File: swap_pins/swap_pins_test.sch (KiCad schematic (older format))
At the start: 6 parts, among them U101 PIC18F452-IP

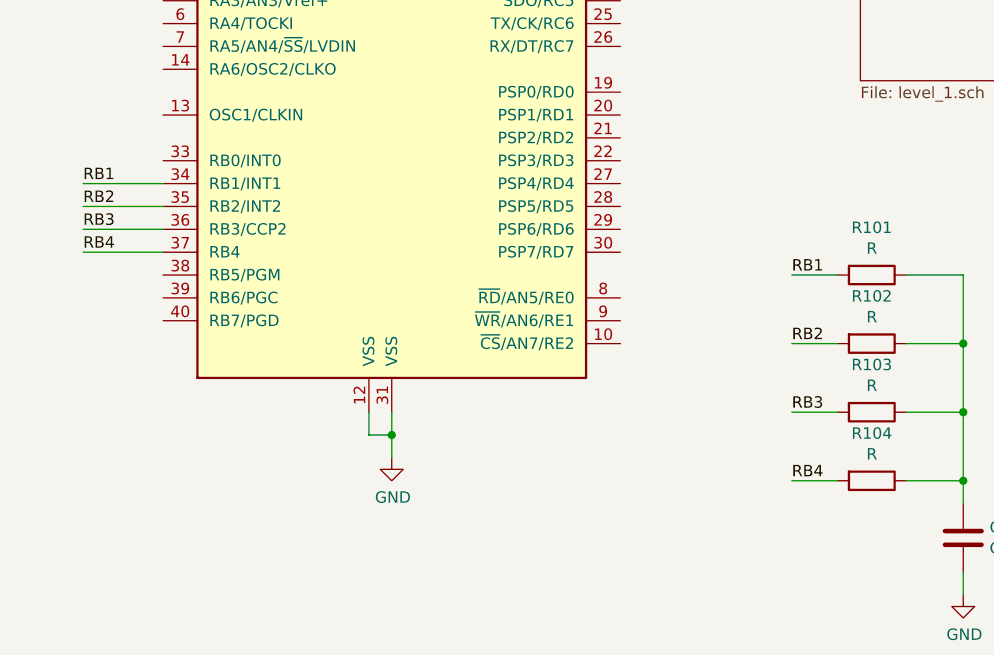
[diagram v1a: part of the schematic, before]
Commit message: changed project to include hierarchical labels also
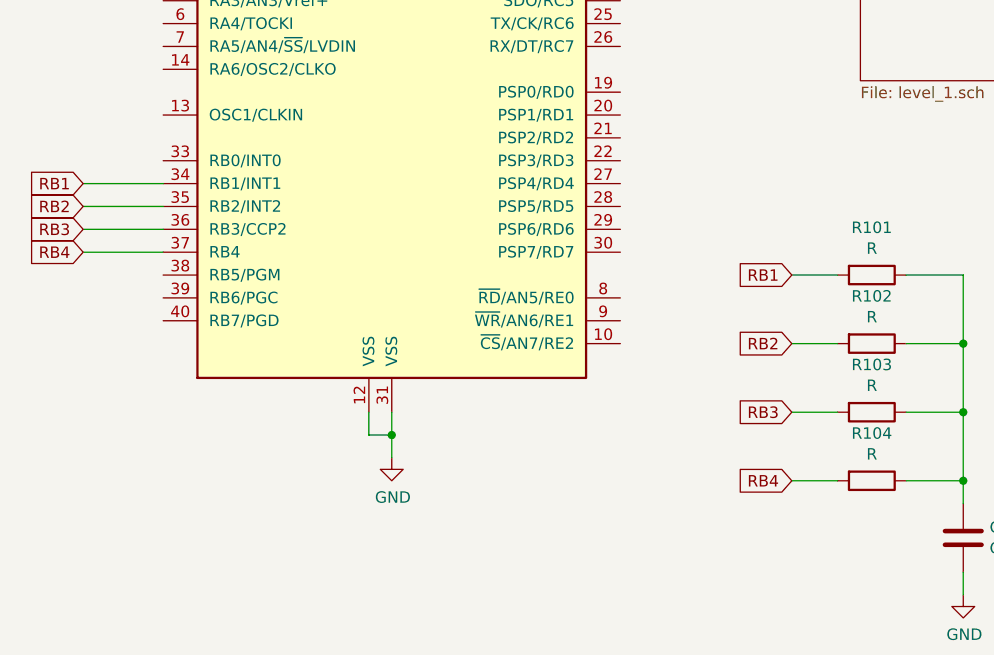
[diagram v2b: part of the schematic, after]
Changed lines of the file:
@@
 	5800 4300 5800 4600
 Connection ~ 5800 4600
-Text Label 5050 4300 0    50   ~ 0
-RB1
-Text Label 5050 4600 0    50   ~ 0
-RB2
-Text Label 5050 4900 0    50   ~ 0
-RB3
-Text Label 5050 5200 0    50   ~ 0
-RB4
 $Comp
 L power:GND #PWR0103
@@
 Wire Wire Line
 	2300 4200 1950 4200
-Text Label 1950 3900 0    50   ~ 0
-RB1
-Text Label 1950 4000 0    50   ~ 0
-RB2
-Text Label 1950 4100 0    50   ~ 0
-RB3
-Text Label 1950 4200 0    50   ~ 0
-RB4
 Wire Wire Line
 	3200 4900 3200 5000
@@
 	1    0    0    -1
 $EndComp
+Text GLabel 1950 3900 0    50   Input ~ 0
+RB1
+Text GLabel 1950 4000 0    50   Input ~ 0
+RB2
+Text GLabel 1950 4100 0    50   Input ~ 0
+RB3
+Text GLabel 1950 4200 0    50   Input ~ 0
+RB4
+Text GLabel 5050 4300 0    50   Input ~ 0
+RB1
+Text GLabel 5050 4600 0    50   Input ~ 0
+RB2
+Text GLabel 5050 4900 0    50   Input ~ 0
+RB3
+Text GLabel 5050 5200 0    50   Input ~ 0
+RB4
 $EndSCHEMATC

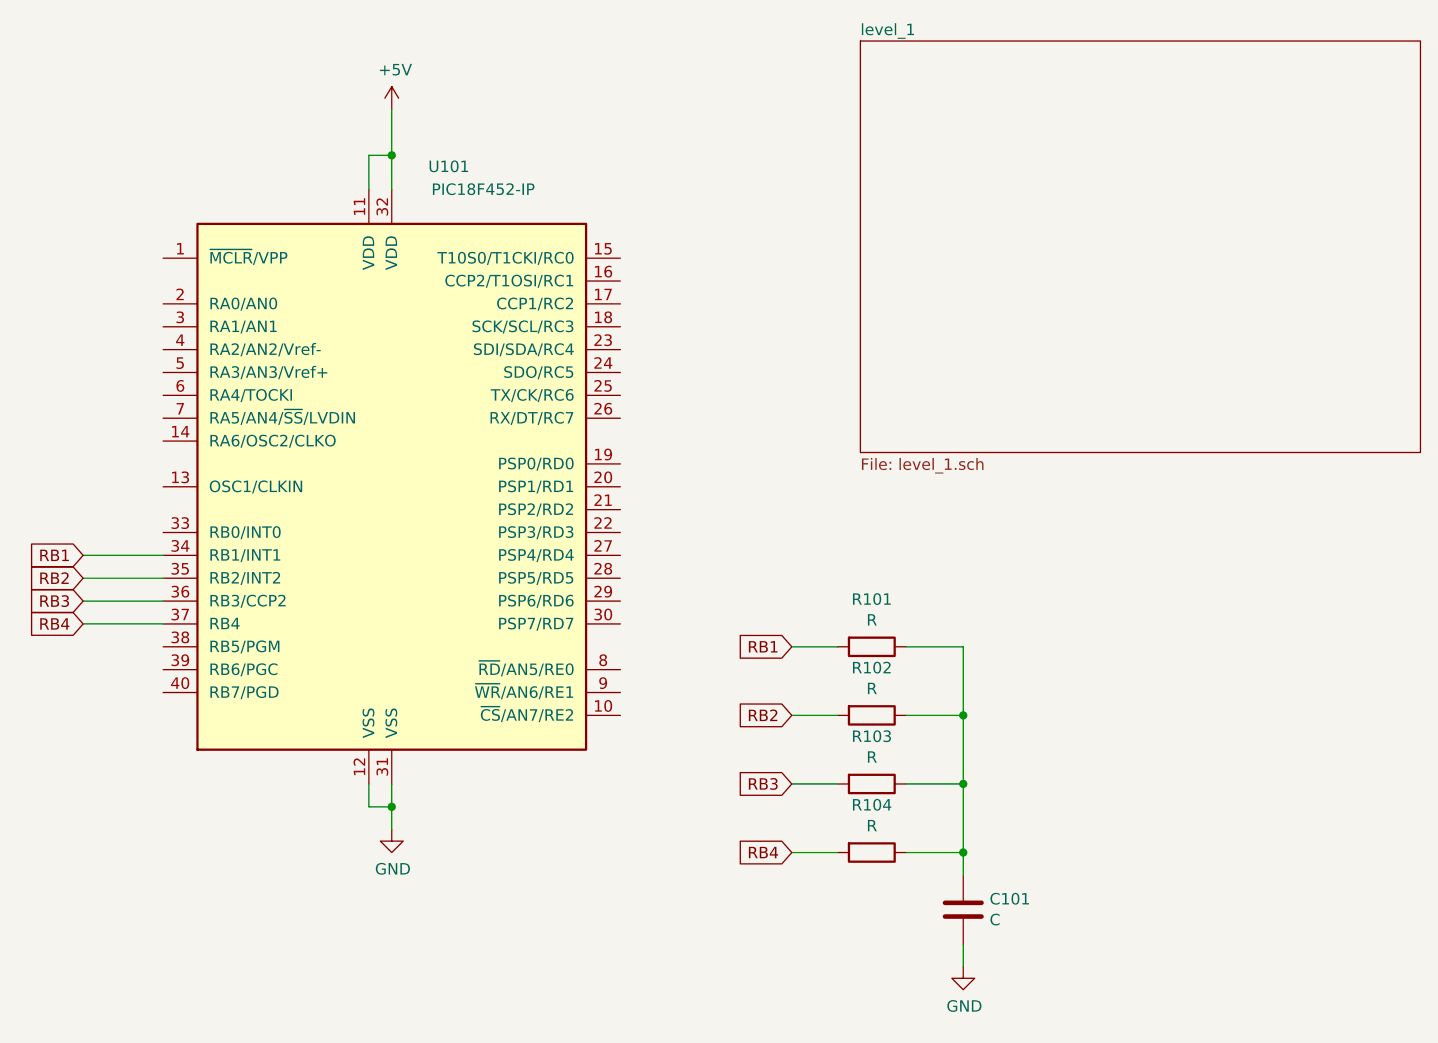
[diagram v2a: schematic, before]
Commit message: Overwritten the plugin with V2 version
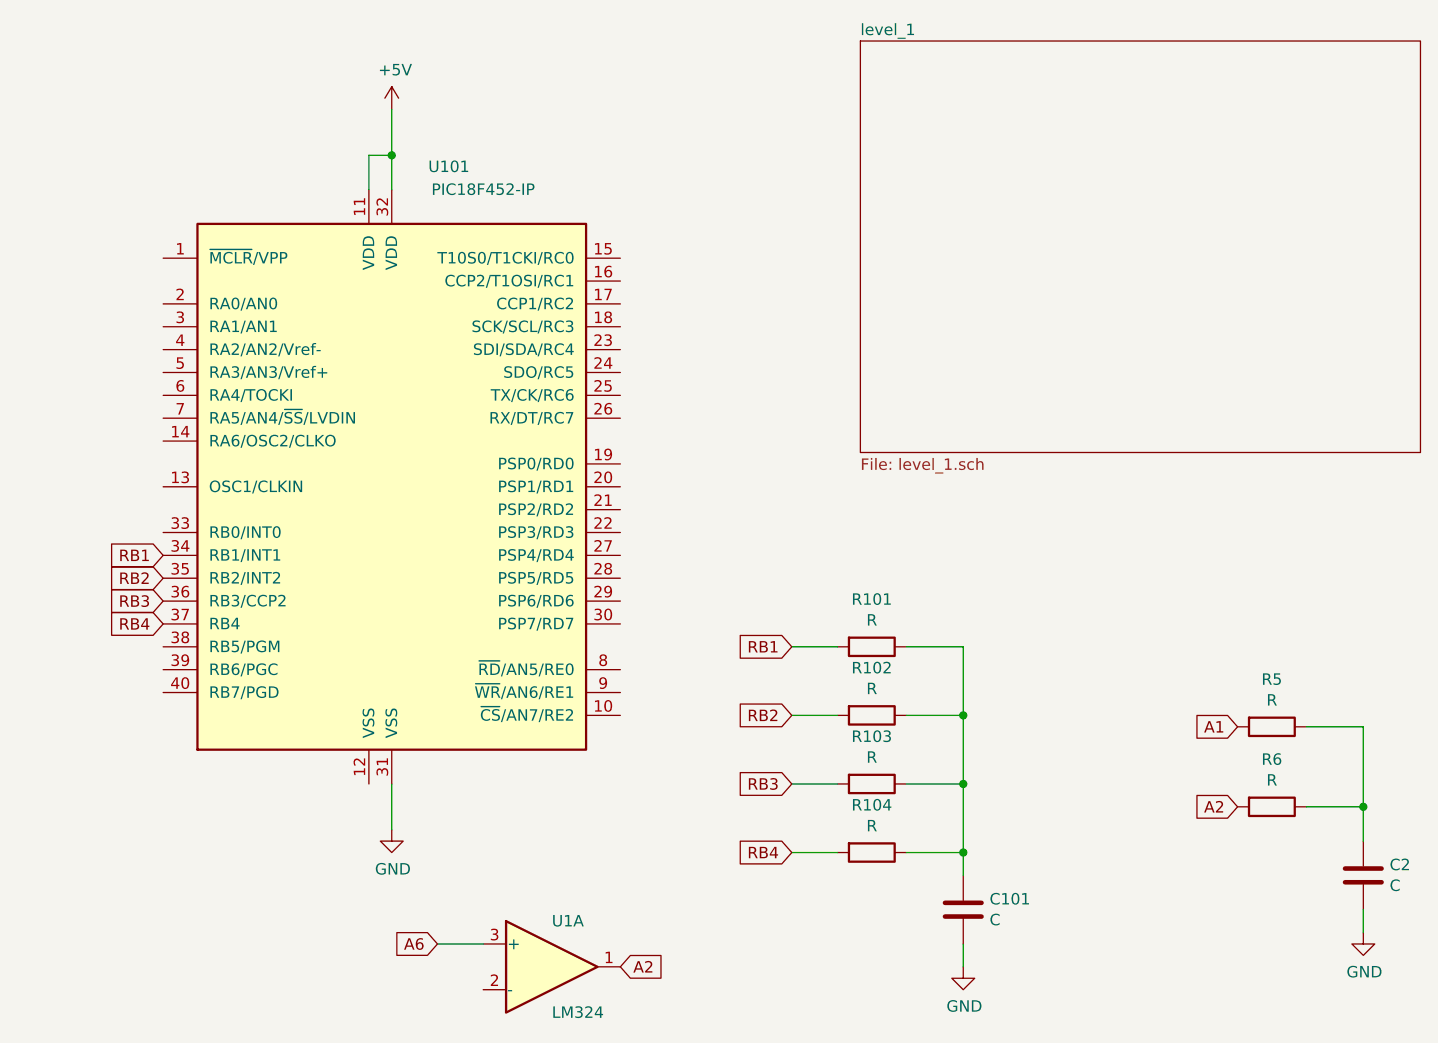
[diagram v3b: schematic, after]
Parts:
- added C2: C, Capacitor_THT:C_Disc_D7.5mm_W5.0mm_P5.00mm, symbol Device:C
- added R5, R6: R, Resistor_THT:R_Axial_DIN0614_L14.3mm_D5.7mm_P20.32mm_Horizontal, symbol Device:R
- added U1: LM324, Package_DIP:DIP-14_W7.62mm, symbol Amplifier_Operational:LM324
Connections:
- net GND: now also C2.2; no longer U101.12 (VSS)
- new net: C2.1, R5.1, R6.1
- new net A1: R5.2
- new net A2: R6.2, U1.1
- new net A6: U1.3 (+)
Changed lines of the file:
@@
 Wire Wire Line
 	5800 5700 5800 5600
-Wire Wire Line
-	2300 3900 1950 3900
-Wire Wire Line
-	2300 4000 1950 4000
-Wire Wire Line
-	2300 4100 1950 4100
-Wire Wire Line
-	2300 4200 1950 4200
-Wire Wire Line
-	3200 4900 3200 5000
-Wire Wire Line
-	3200 5000 3300 5000
-Wire Wire Line
-	3300 5000 3300 5100
-Wire Wire Line
-	3300 4900 3300 5000
-Connection ~ 3300 5000
 $Comp
 L power:GND #PWR0102
@@
 	1    0    0    -1
 $EndComp
-Text GLabel 1950 3900 0    50   Input ~ 0
+Text GLabel 2300 3900 0    50   Input ~ 0
 RB1
-Text GLabel 1950 4000 0    50   Input ~ 0
+Text GLabel 2300 4000 0    50   Input ~ 0
 RB2
-Text GLabel 1950 4100 0    50   Input ~ 0
+Text GLabel 2300 4100 0    50   Input ~ 0
 RB3
-Text GLabel 1950 4200 0    50   Input ~ 0
+Text GLabel 2300 4200 0    50   Input ~ 0
 RB4
 Text GLabel 5050 4300 0    50   Input ~ 0
@@
 Text GLabel 5050 5200 0    50   Input ~ 0
 RB4
+Wire Wire Line
+	3300 4900 3300 5100
+$Comp
+L Amplifier_Operational:LM324 U1
+U 1 1 5B34A98C
+P 4000 5700
+F 0 "U1" H 4000 5900 50  0000 L CNN
+F 1 "LM324" H 4000 5500 50  0000 L CNN
+F 2 "Package_DIP:DIP-14_W7.62mm" H 3950 5800 50  0001 C CNN
+F 3 "http://www.ti.com/lit/ds/symlink/lm2902-n.pdf" H 4050 5900 50  0001 C CNN
+	1    4000 5700
+	1    0    0    -1
+$EndComp
+Text GLabel 4300 5700 2    50   Input ~ 0
+A2
+$Comp
+L Device:R R5
+U 1 1 5B34BDEE
+P 7150 4650
+F 0 "R5" V 6943 4650 50  0000 C CNN
+F 1 "R" V 7034 4650 50  0000 C CNN
+F 2 "Resistor_THT:R_Axial_DIN0614_L14.3mm_D5.7mm_P20.32mm_Horizontal" V 7080 4650 50  0001 C CNN
+F 3 "~" H 7150 4650 50  0001 C CNN
+	1    7150 4650
+	0    1    1    0
+$EndComp
+$Comp
+L Device:R R6
+U 1 1 5B34BE50
+P 7150 5000
+F 0 "R6" V 6943 5000 50  0000 C CNN
+F 1 "R" V 7034 5000 50  0000 C CNN
+F 2 "Resistor_THT:R_Axial_DIN0614_L14.3mm_D5.7mm_P20.32mm_Horizontal" V 7080 5000 50  0001 C CNN
+F 3 "~" H 7150 5000 50  0001 C CNN
+	1    7150 5000
+	0    1    1    0
+$EndComp
+$Comp
+L Device:C C2
+U 1 1 5B34BE9A
+P 7550 5300
+F 0 "C2" H 7665 5346 50  0000 L CNN
+F 1 "C" H 7665 5255 50  0000 L CNN
+F 2 "Capacitor_THT:C_Disc_D7.5mm_W5.0mm_P5.00mm" H 7588 5150 50  0001 C CNN
+F 3 "~" H 7550 5300 50  0001 C CNN
+	1    7550 5300
+	1    0    0    -1
+$EndComp
+$Comp
+L power:GND #PWR01
+U 1 1 5B34BEF8
+P 7550 5550
+F 0 "#PWR01" H 7550 5300 50  0001 C CNN
+F 1 "GND" H 7555 5377 50  0000 C CNN
+F 2 "" H 7550 5550 50  0001 C CNN
+F 3 "" H 7550 5550 50  0001 C CNN
+	1    7550 5550
+	1    0    0    -1
+$EndComp
+Wire Wire Line
+	7550 5450 7550 5550
+Wire Wire Line
+	7550 5150 7550 5000
+Wire Wire Line
+	7550 5000 7300 5000
+Wire Wire Line
+	7300 4650 7550 4650
+Wire Wire Line
+	7550 4650 7550 5000
+Connection ~ 7550 5000
+Text GLabel 7000 4650 0    50   Input ~ 0
+A1
+Text GLabel 7000 5000 0    50   Input ~ 0
+A2
+Wire Wire Line
+	3700 5600 3500 5600
+Text GLabel 3500 5600 0    50   Input ~ 0
+A6
 $EndSCHEMATC

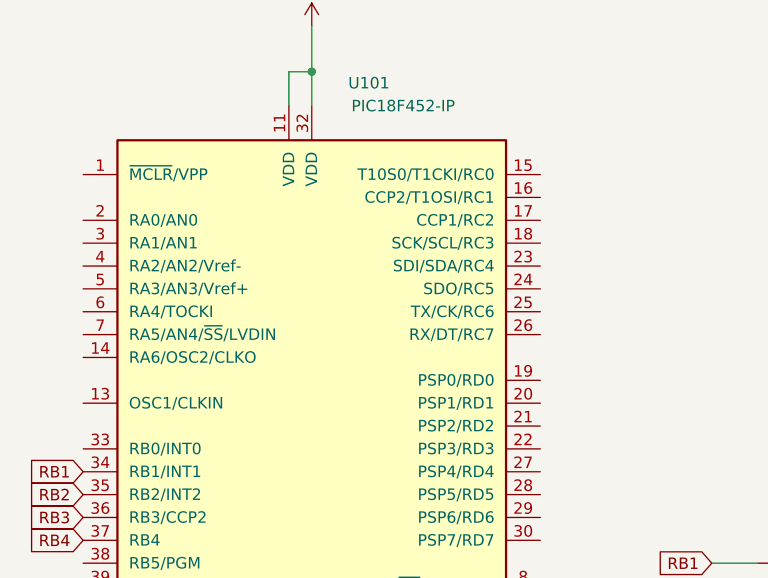
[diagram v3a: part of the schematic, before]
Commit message: Gracefully handle common pins swapping Fixed an additional bug
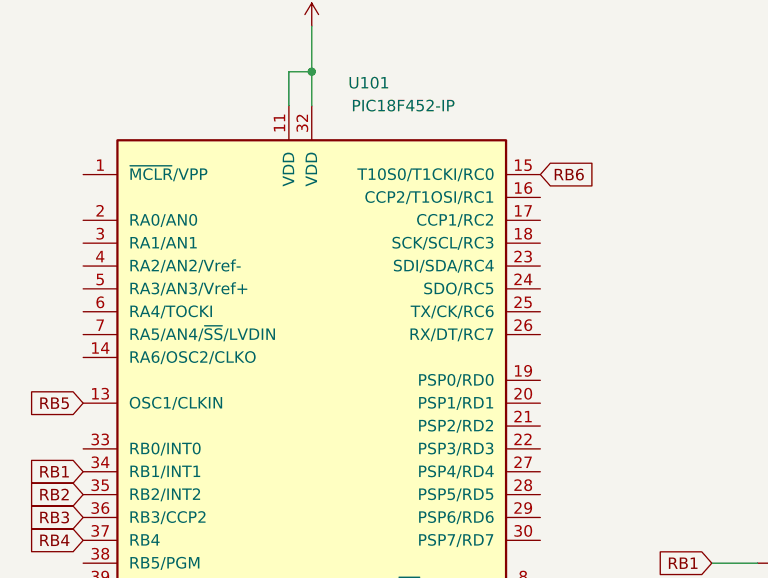
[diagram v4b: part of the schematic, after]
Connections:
- net RB5: now reaches U101.13 (OSC1/CLKIN)
- net RB6: now reaches U101.15 (T10S0/T1CKI/RC0)
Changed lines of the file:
@@
 Text GLabel 3500 5600 0    50   Input ~ 0
 A6
+Text GLabel 2300 3600 0    50   Input ~ 0
+RB5
+Text GLabel 4300 2600 2    50   Input ~ 0
+RB6
 $EndSCHEMATC
